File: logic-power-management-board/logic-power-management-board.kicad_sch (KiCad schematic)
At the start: 59 parts, among them IC1 MCP2562, J1 Conn_01x02, J2 Conn_01x02, J3 Conn_01x02, J4 Conn_01x04, J5 Conn_01x04, J6 Conn_01x02, J7 Conn_01x04, J8 Conn_01x04_Pin, Q1 RS6L120BGTB1, Q2 RS6L120BGTB1, Q3 RS6L120BGTB1, SW2 SW_Push, U1 LM5050-1, U2 LM5050-1, U3 STM32G431K8Tx, U4 LM5050-1, U5 NJM12888F33

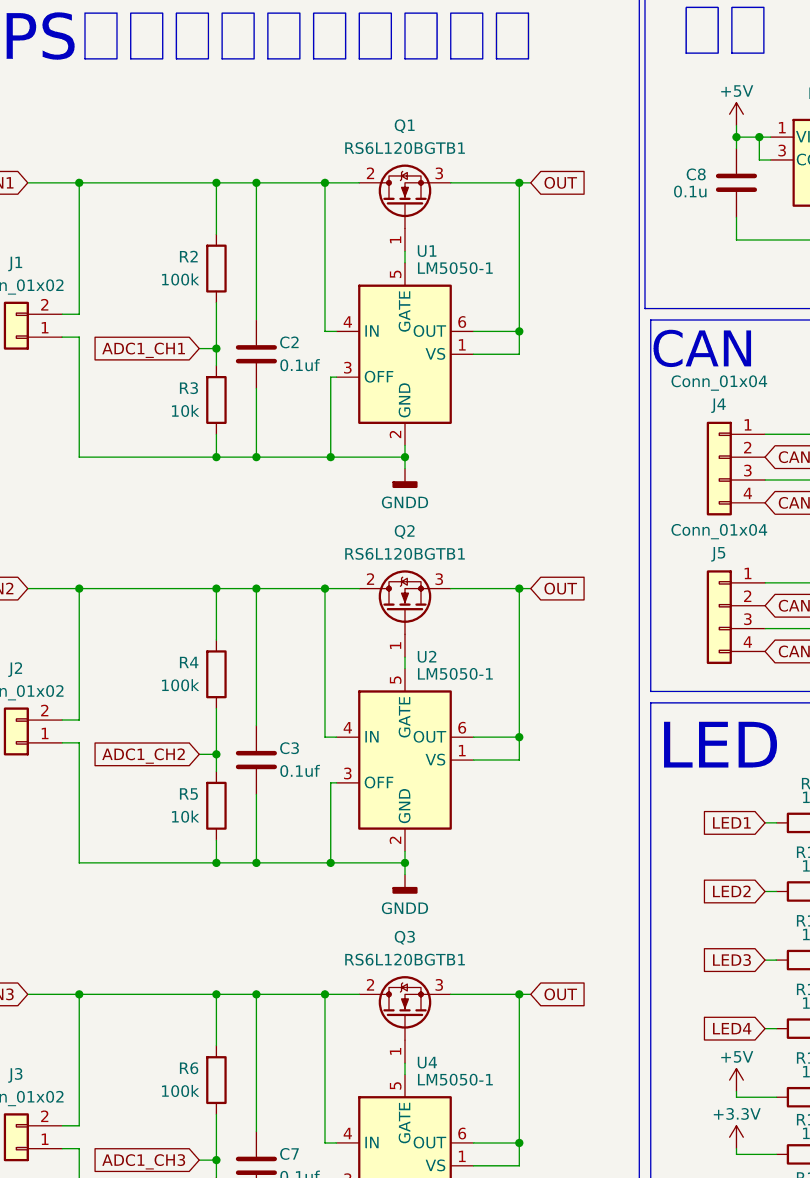
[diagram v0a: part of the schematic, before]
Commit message: FETの向きが逆だったので修正
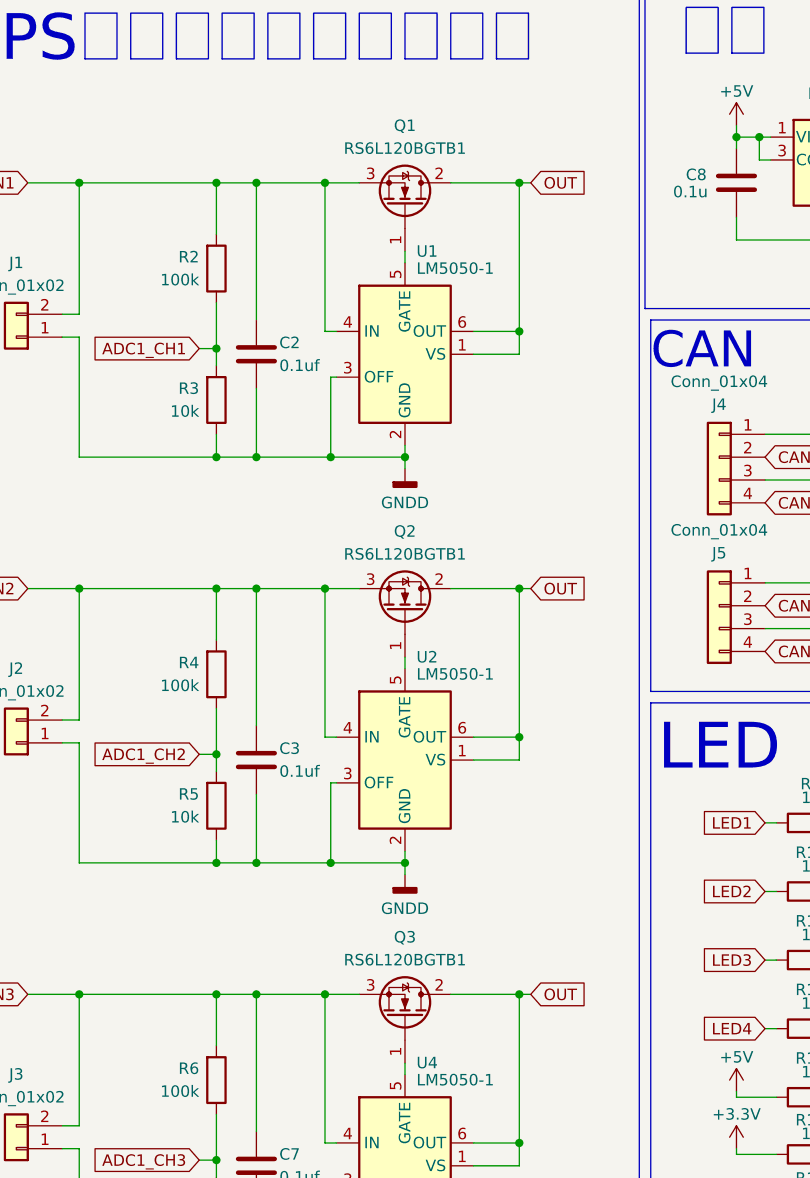
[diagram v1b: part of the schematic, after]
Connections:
- net IN1: now also Q1.3 (S); no longer Q1.2 (D)
- net IN2: now also Q2.3 (S); no longer Q2.2 (D)
- net IN3: now also Q3.3 (S); no longer Q3.2 (D)
- net OUT: now also Q1.2 (D), Q2.2 (D), Q3.2 (D); no longer Q1.3 (S), Q2.3 (S), Q3.3 (S)
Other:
- moved on the sheet: Q1, Q2, Q3
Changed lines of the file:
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@@
 	(symbol
 		(lib_id "Device:Q_NMOS_GDS")
-		(at 71.12 37.465 90)
-		(unit 1)
-		(exclude_from_sim no)
-		(in_bom yes)
-		(on_board yes)
-		(dnp no)
-		(fields_autoplaced yes)
+		(at 71.12 37.465 270)
+		(mirror x)
+		(unit 1)
+		(exclude_from_sim no)
+		(in_bom yes)
+		(on_board yes)
+		(dnp no)
 		(property "Reference" "Q1"
 			(at 71.12 28.575 90)
@@
 		)
 		(property "Footprint" "0Ikedalibrary:SOP_Advance"
-			(at 68.58 32.385 0)
+			(at 73.66 32.385 0)
 			(effects
 				(font
@@
 	(symbol
 		(lib_id "Device:Q_NMOS_GDS")
-		(at 71.12 82.55 90)
-		(unit 1)
-		(exclude_from_sim no)
-		(in_bom yes)
-		(on_board yes)
-		(dnp no)
-		(fields_autoplaced yes)
+		(at 71.12 82.55 270)
+		(mirror x)
+		(unit 1)
+		(exclude_from_sim no)
+		(in_bom yes)
+		(on_board yes)
+		(dnp no)
 		(property "Reference" "Q2"
 			(at 71.12 73.66 90)
@@
 		)
 		(property "Footprint" "0Ikedalibrary:SOP_Advance"
-			(at 68.58 77.47 0)
+			(at 73.66 77.47 0)
 			(effects
 				(font
@@
 	(symbol
 		(lib_id "Device:Q_NMOS_GDS")
-		(at 71.12 127.635 90)
-		(unit 1)
-		(exclude_from_sim no)
-		(in_bom yes)
-		(on_board yes)
-		(dnp no)
-		(fields_autoplaced yes)
+		(at 71.12 127.635 270)
+		(mirror x)
+		(unit 1)
+		(exclude_from_sim no)
+		(in_bom yes)
+		(on_board yes)
+		(dnp no)
 		(property "Reference" "Q3"
 			(at 71.12 118.745 90)
@@
 		)
 		(property "Footprint" "0Ikedalibrary:SOP_Advance"
-			(at 68.58 122.555 0)
-			(effects
-				(font
+			(at 73.66 122.555 0)
+			(effects
+				(font

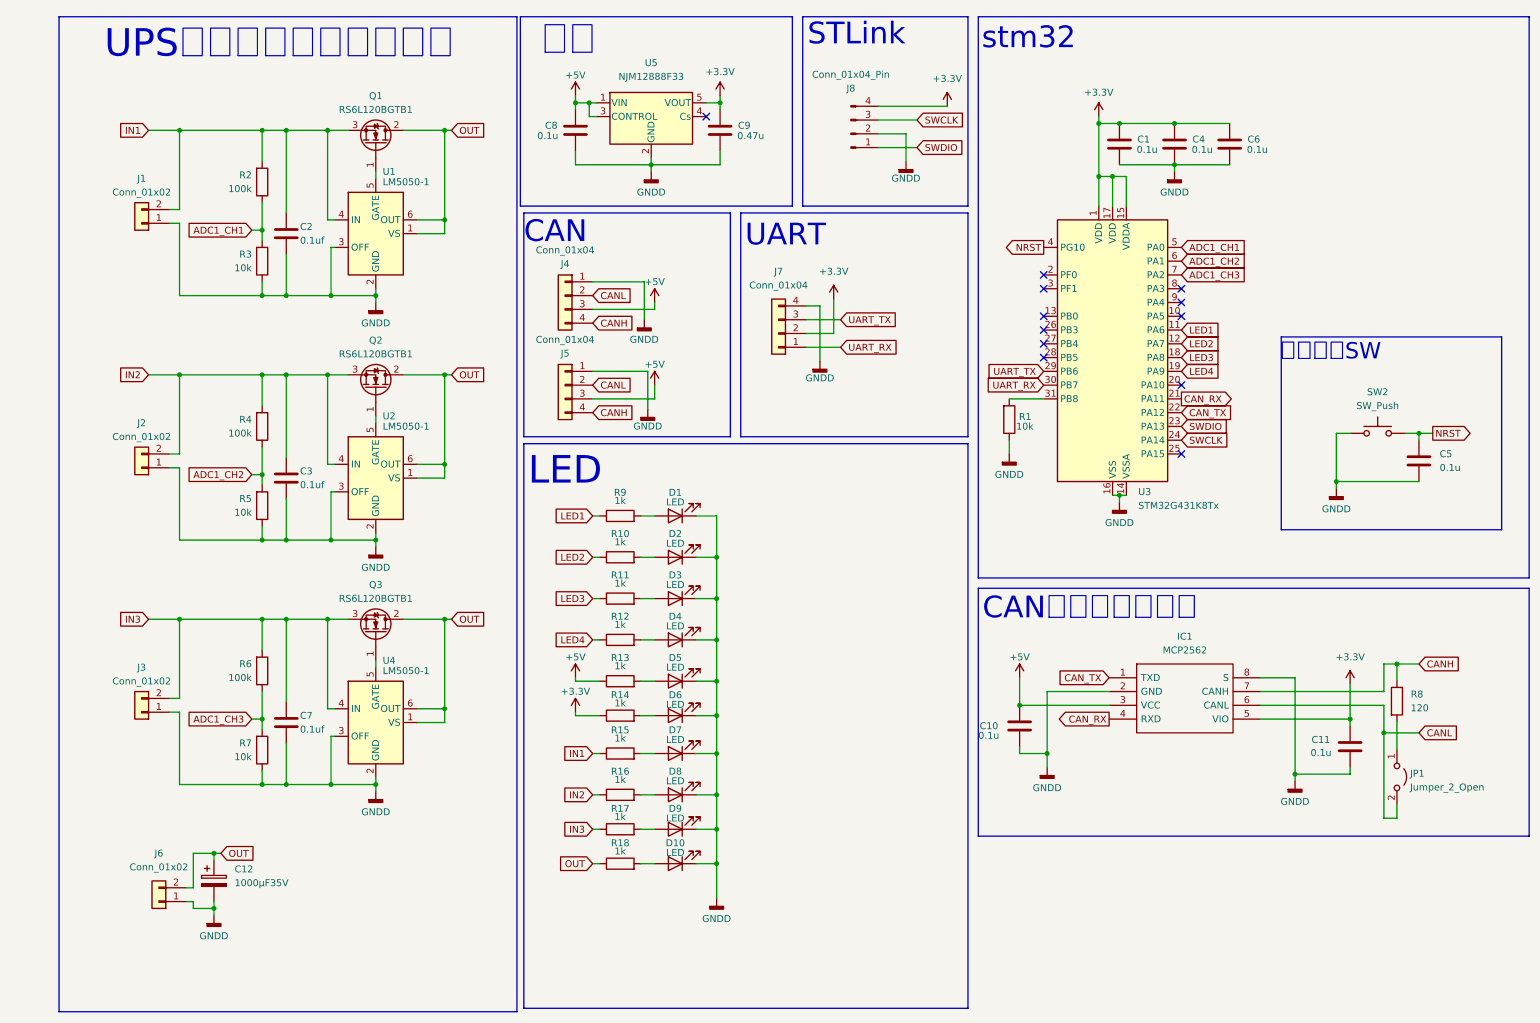
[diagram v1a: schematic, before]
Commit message: PCB完成(ビア、シルクを除く)
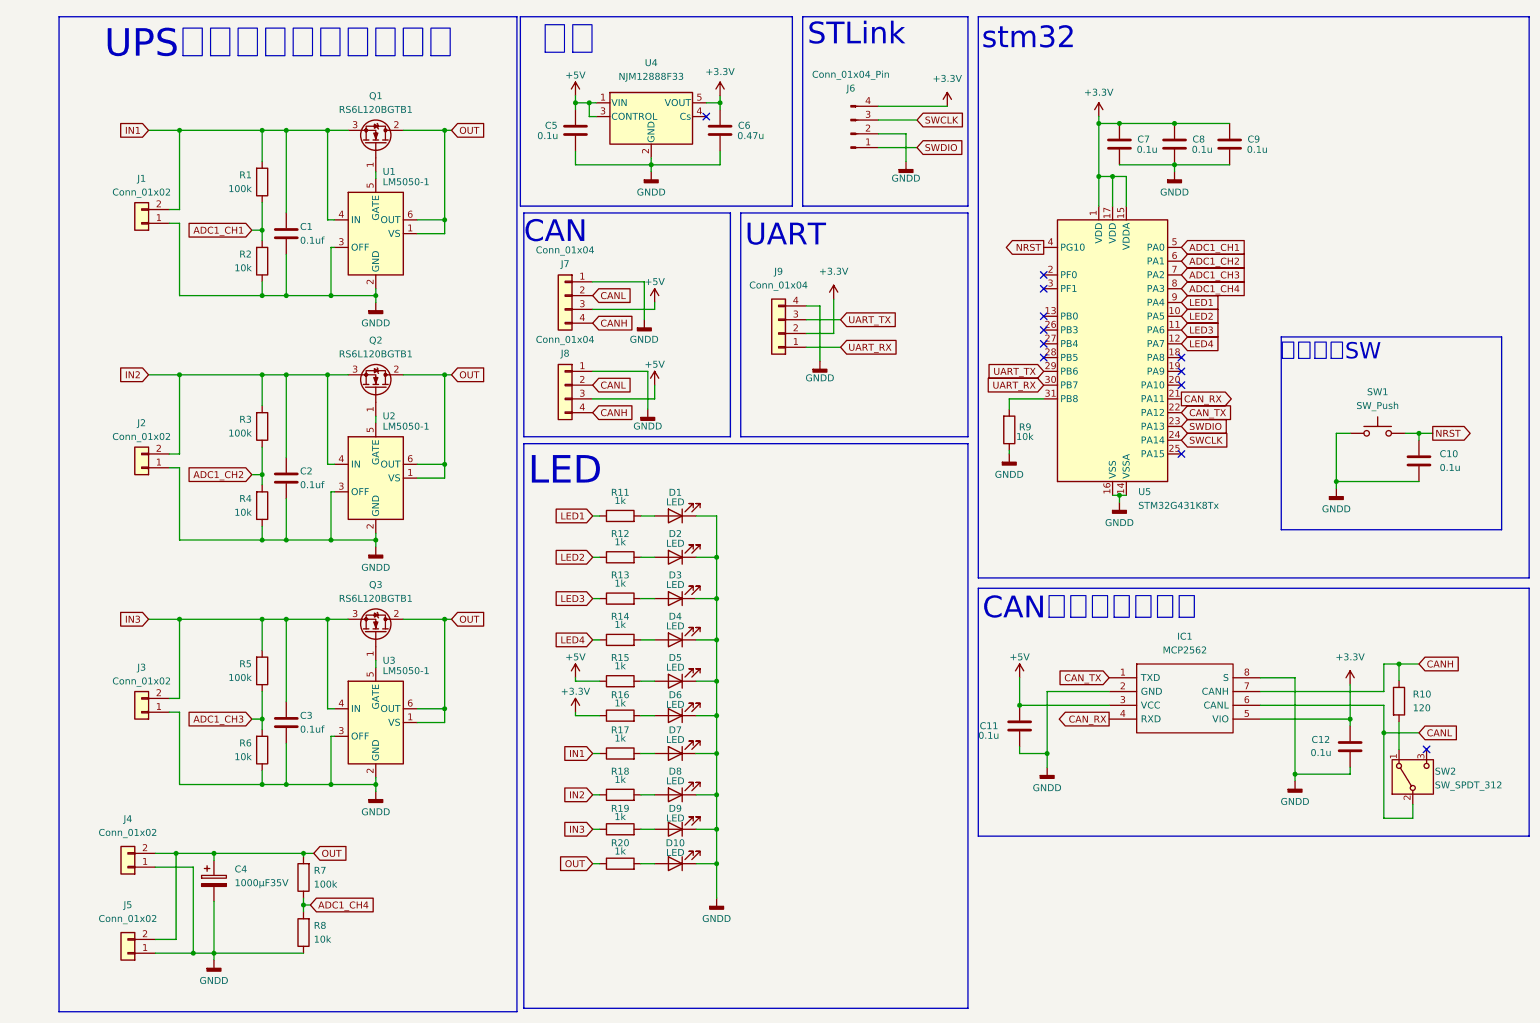
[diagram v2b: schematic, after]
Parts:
- removed JP1: Jumper_2_Open, TestPoint:TestPoint_2Pads_Pitch2.54mm_Drill0.8mm, symbol Jumper:Jumper_2_Open
- added J5: Conn_01x02, 0Ikedalibrary:AMASS_XT60PW-F_1x02_P7.20mm_Horizontal, symbol Connector_Generic:Conn_01x02
- added R7: 100k, Resistor_SMD:R_0603_1608Metric_Pad0.98x0.95mm_HandSolder, symbol Device:R
- added R8: 10k, Resistor_SMD:R_0603_1608Metric_Pad0.98x0.95mm_HandSolder, symbol Device:R
- added SW2: SW_SPDT_312, 0Ikedalibrary:CJS1200A1, symbol Switch:SW_SPDT_312
- J9: renamed from J7; footprint Connector_JST:JST_XH_S4B-XH-A_1x04_P2.50mm_Horizontal -> Connector_JST:JST_XH_B4B-XH-A_1x04_P2.50mm_Vertical
- renumbered C2 to C1, C5 to C10, C10 to C11, C11 to C12, C3 to C2, C7 to C3, C12 to C4, C8 to C5, C9 to C6, C1 to C7, C4 to C8, C6 to C9, J6 to J4, J8 to J6, J4 to J7, J5 to J8, R2 to R1, R8 to R10, R9 to R11, R10 to R12, R11 to R13, R12 to R14, R13 to R15, R14 to R16, R15 to R17, R16 to R18, R17 to R19, R3 to R2, R18 to R20, R4 to R3, R5 to R4, R6 to R5, R7 to R6, R1 to R9, SW2 to SW1, U4 to U3, U5 to U4, U3 to U5
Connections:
- net CANL: now also SW2.2 (B)
- net GNDD: now also J5.1 (Pin_1), R8.1
- net LED1: now also U5.9 (PA4); no longer U5.11 (PA6)
- net LED2: now also U5.10 (PA5); no longer U5.12 (PA7)
- net LED3: now also U5.11 (PA6); no longer U5.18 (PA8)
- net LED4: now also U5.12 (PA7); no longer U5.19 (PA9)
- net OUT: now also J5.2 (Pin_2), R7.2
- net at R10.2: now also SW2.1 (A)
- net ADC1_CH4: now reaches U5.8 (PA3)
- net ADC1_CH4: now also R7.1, R8.2
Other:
- moved on the sheet: J4, R9

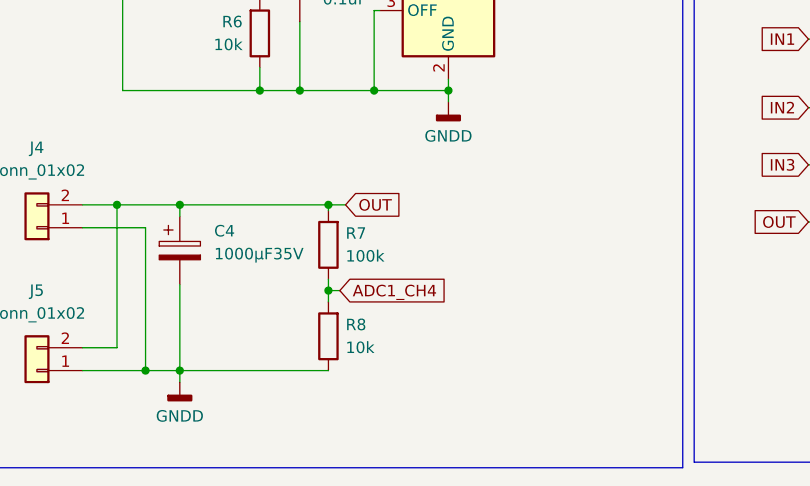
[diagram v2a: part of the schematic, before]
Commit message: コンデンサー追加、シルク修正
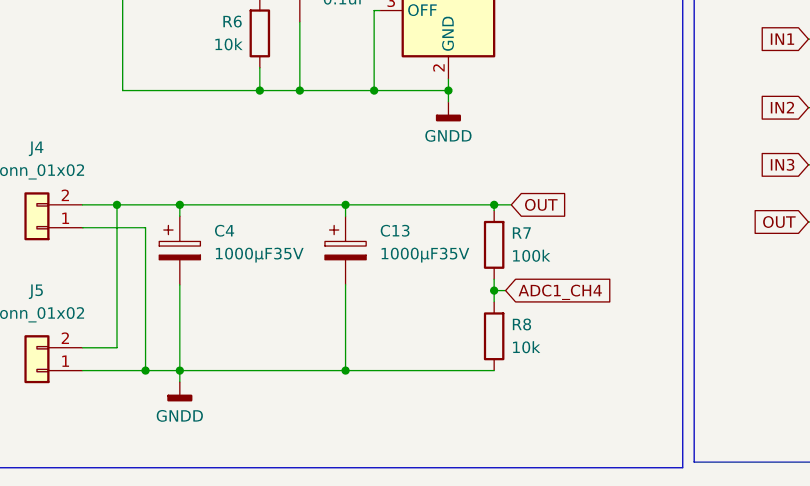
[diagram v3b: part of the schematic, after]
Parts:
- added C13: 1000μF35V, Capacitor_THT:CP_Radial_D12.5mm_P5.00mm, symbol Device:C_Polarized
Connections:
- net GNDD: now also C13.2
- net OUT: now also C13.1
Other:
- moved on the sheet: R7, R8
